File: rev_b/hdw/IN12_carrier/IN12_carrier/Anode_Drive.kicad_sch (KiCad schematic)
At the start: 36 parts, among them Q1001 MMSTA92, Q1002 MMSTA92, Q1003 MMSTA42, Q1004 MMSTA42, Q1005 MMSTA92, Q1006 MMSTA92, Q1007 MMSTA42, Q1008 MMSTA42, Q1009 MMSTA92, Q1010 MMSTA92, Q1011 MMSTA42, Q1012 MMSTA42

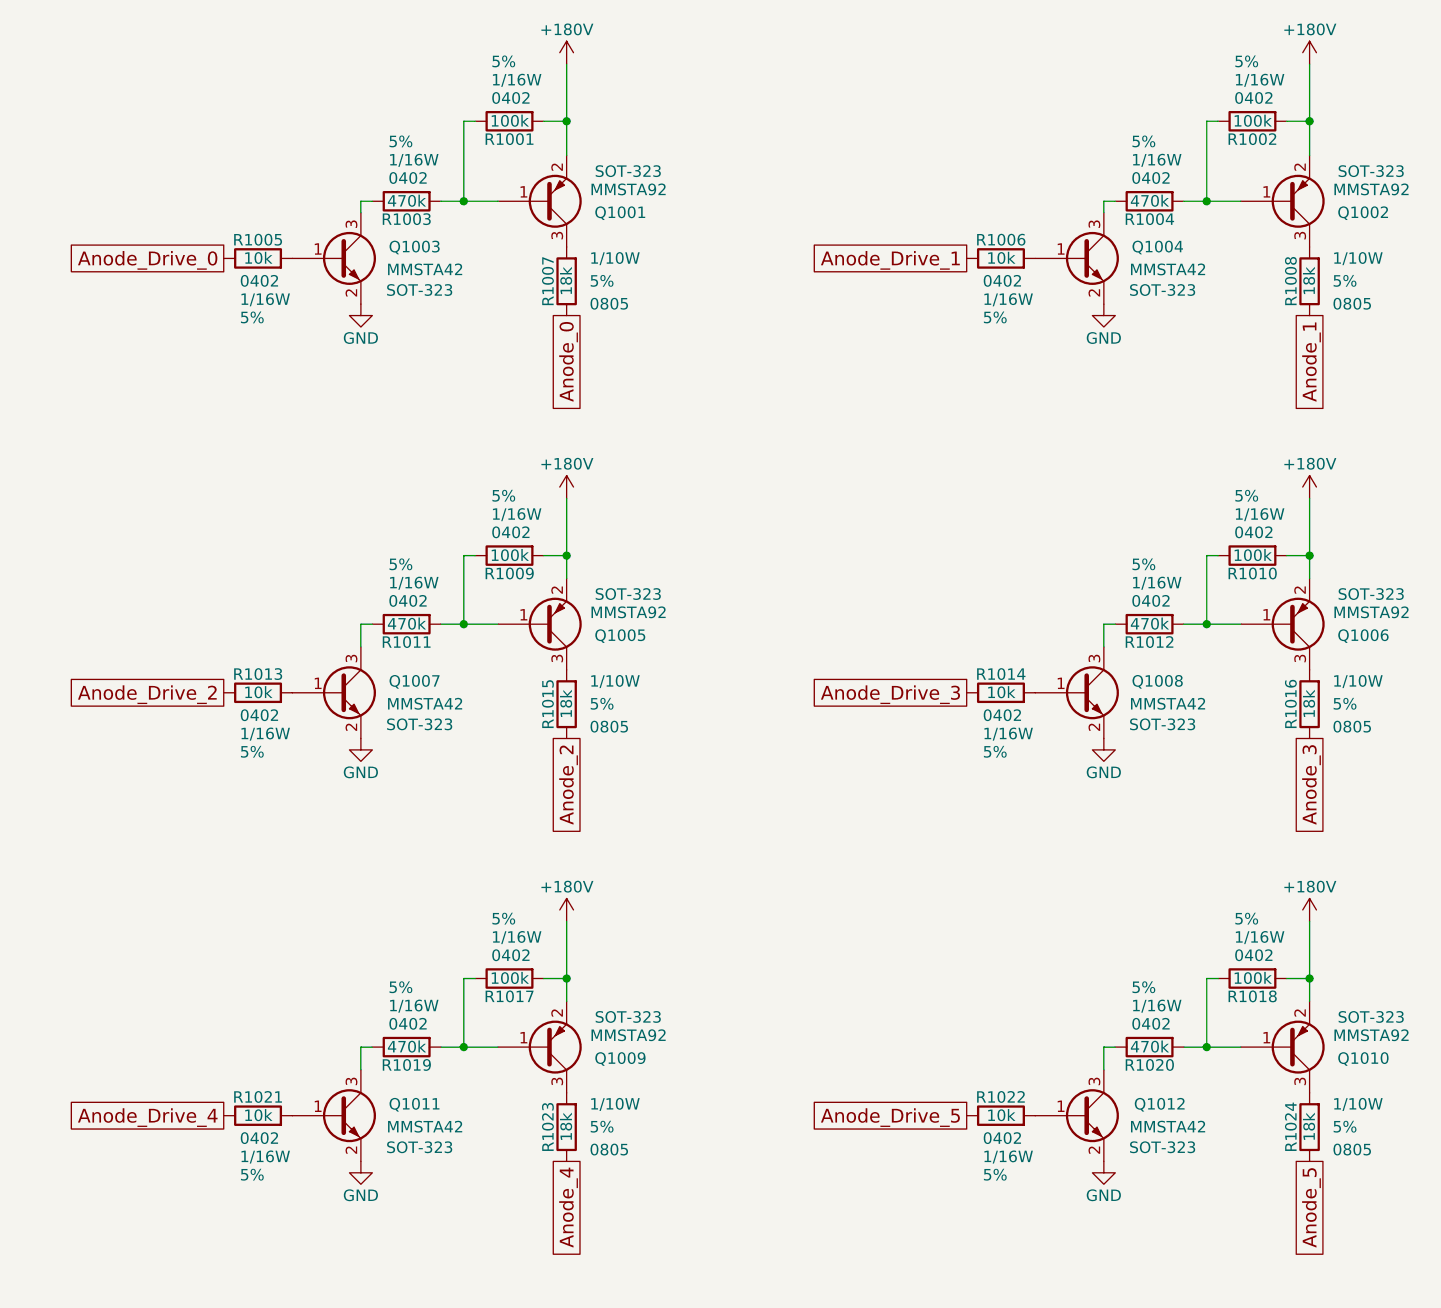
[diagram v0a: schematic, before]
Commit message: updated footprints, ran some DRC
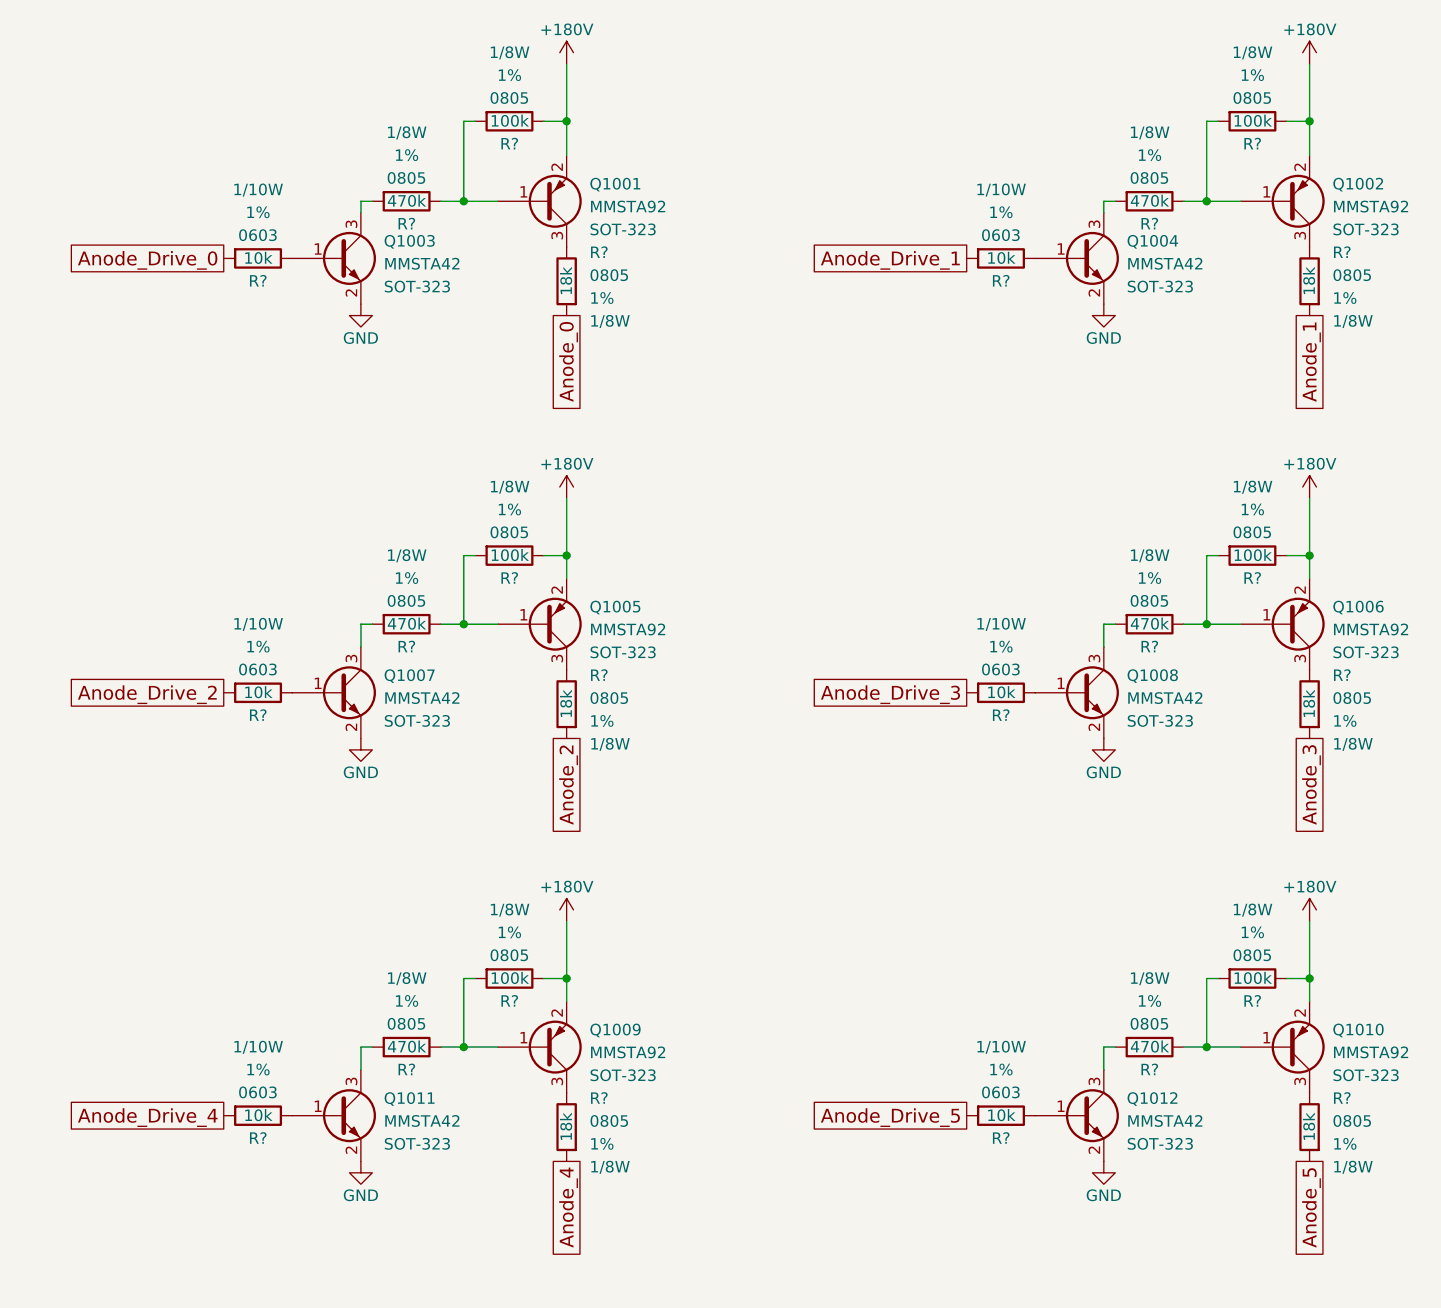
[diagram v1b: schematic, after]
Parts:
- removed R1001, R1002, R1009, R1010, R1017, R1018: 100k, Resistors_SMD:R_0402, symbol Nixie-Clock-rescue:R
- removed R1003, R1004, R1011, R1012, R1019, R1020: 470k, Resistors_SMD:R_0402, symbol Nixie-Clock-rescue:R
- removed R1005, R1006, R1013, R1014, R1021, R1022: 10k, Resistors_SMD:R_0402, symbol Nixie-Clock-rescue:R
- removed R1007, R1008, R1015, R1016, R1023, R1024: 18k, Resistors_SMD:R_0805, symbol Nixie-Clock-rescue:R
- added R? (x6): 470k, Resistors_SMD:R_0805, symbol Custom Library:R_Custom
- added R? (x6): 18k, Resistors_SMD:R_0805, symbol Custom Library:R_Custom
- added R? (x6): 10k, Resistors_SMD:R_0603, symbol Custom Library:R_Custom
- added R? (x6): 100k, Resistors_SMD:R_0805, symbol Custom Library:R_Custom
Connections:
- net +180V: now also R?.2, R?.2, R?.2, R?.2, R?.2, R?.2
- net Anode_0: now also R?.1
- net Anode_1: now also R?.1
- net Anode_2: now also R?.1
- net Anode_3: now also R?.1
- net Anode_4: now also R?.1
- net Anode_5: now also R?.1
- net Anode_Drive_0: now also R?.1
- net Anode_Drive_1: now also R?.1
- net Anode_Drive_2: now also R?.1
- net Anode_Drive_3: now also R?.1
- net Anode_Drive_4: now also R?.1
- net Anode_Drive_5: now also R?.1
- net at Q1010.1 (B): now also R?.1, R?.2
- net at Q1009.3 (C): now also R?.2
- net at Q1005.1 (B): now also R?.1, R?.2
- net at Q1008.1 (B): now also R?.2
- net at Q1008.3 (C): now also R?.1
- net at Q1005.3 (C): now also R?.2
- net at Q1009.1 (B): now also R?.1, R?.2
- net at Q1004.3 (C): now also R?.1
- net at Q1002.1 (B): now also R?.1, R?.2
- net at Q1002.3 (C): now also R?.2
- net at Q1003.1 (B): now also R?.2
- net at Q1003.3 (C): now also R?.1
- net at Q1007.3 (C): now also R?.1
- net at Q1011.3 (C): now also R?.1
- net at Q1011.1 (B): now also R?.2
- net at Q1007.1 (B): now also R?.2
- net at Q1006.3 (C): now also R?.2
- net at Q1006.1 (B): now also R?.1, R?.2
- net at Q1001.1 (B): now also R?.1, R?.2
- net at Q1004.1 (B): now also R?.2
- net at Q1012.3 (C): now also R?.1
- net at Q1010.3 (C): now also R?.2
- net at Q1001.3 (C): now also R?.2
- net at Q1012.1 (B): now also R?.2

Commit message: annotated, started arranging parts for IN12 carrier
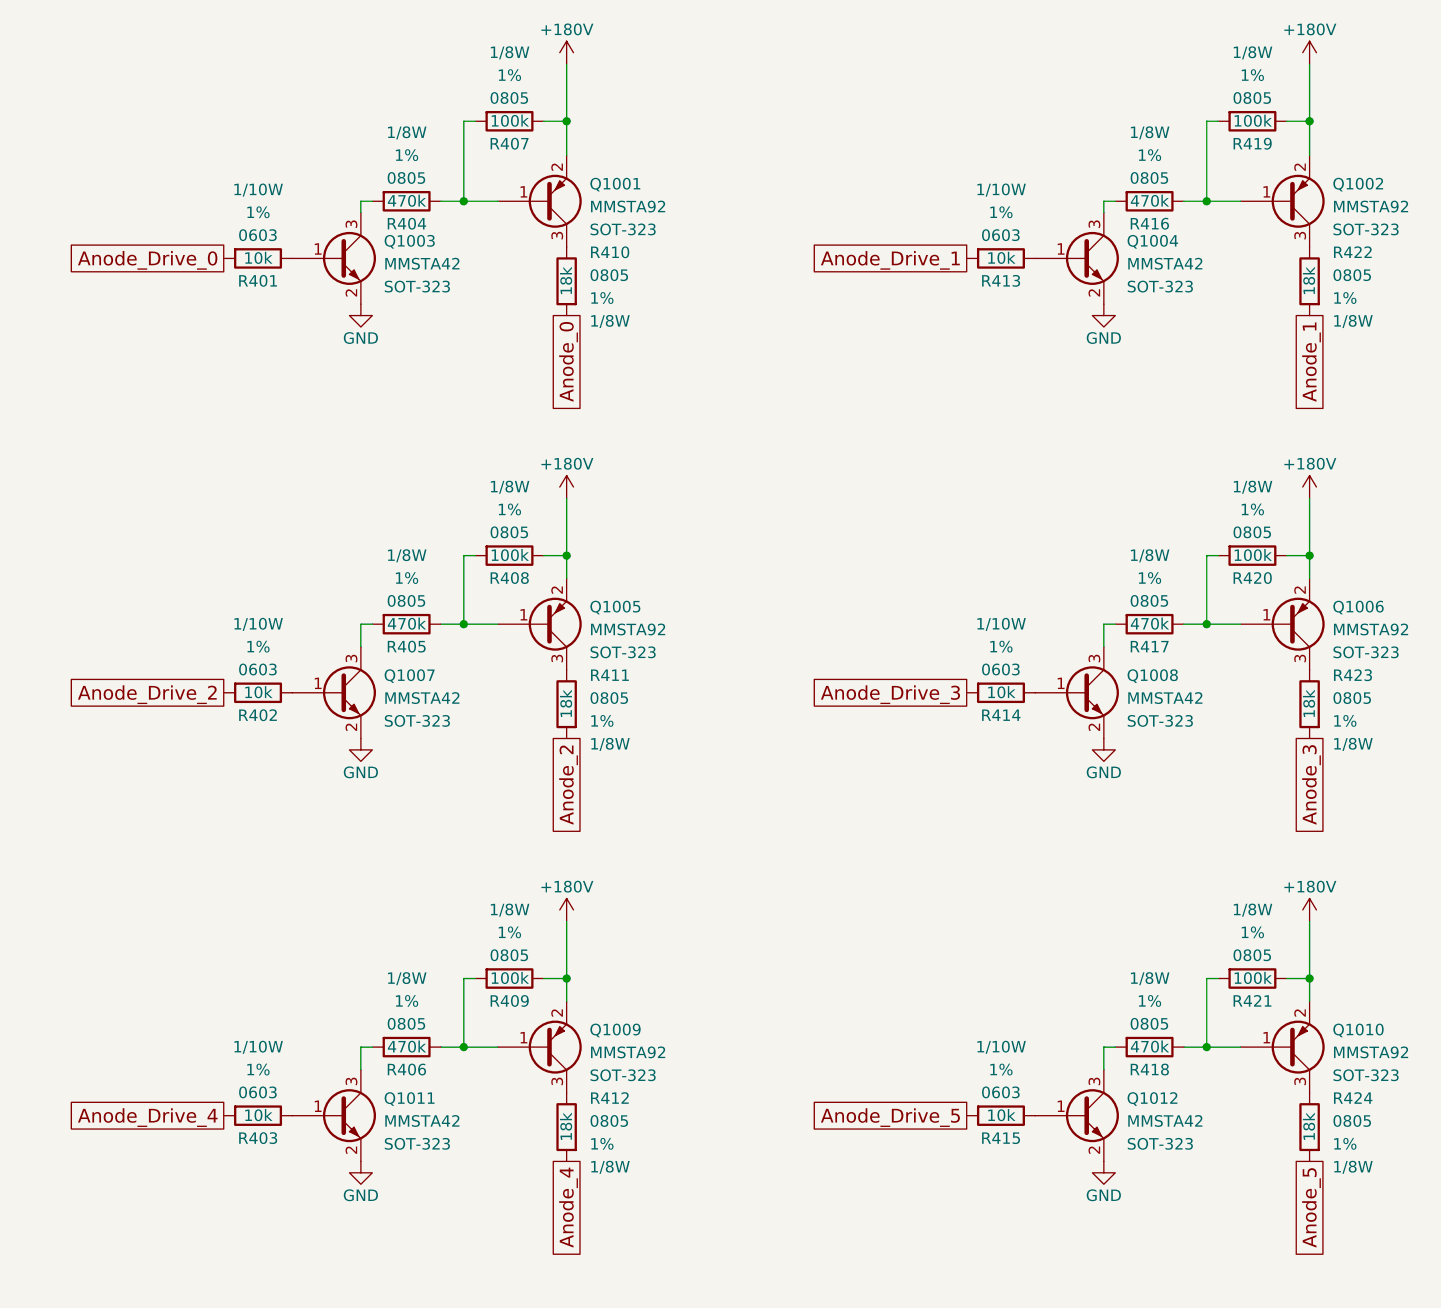
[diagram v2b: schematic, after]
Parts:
- gave numbers to parts that had none: 24

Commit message: lots of placement progress on IN12 carrier board
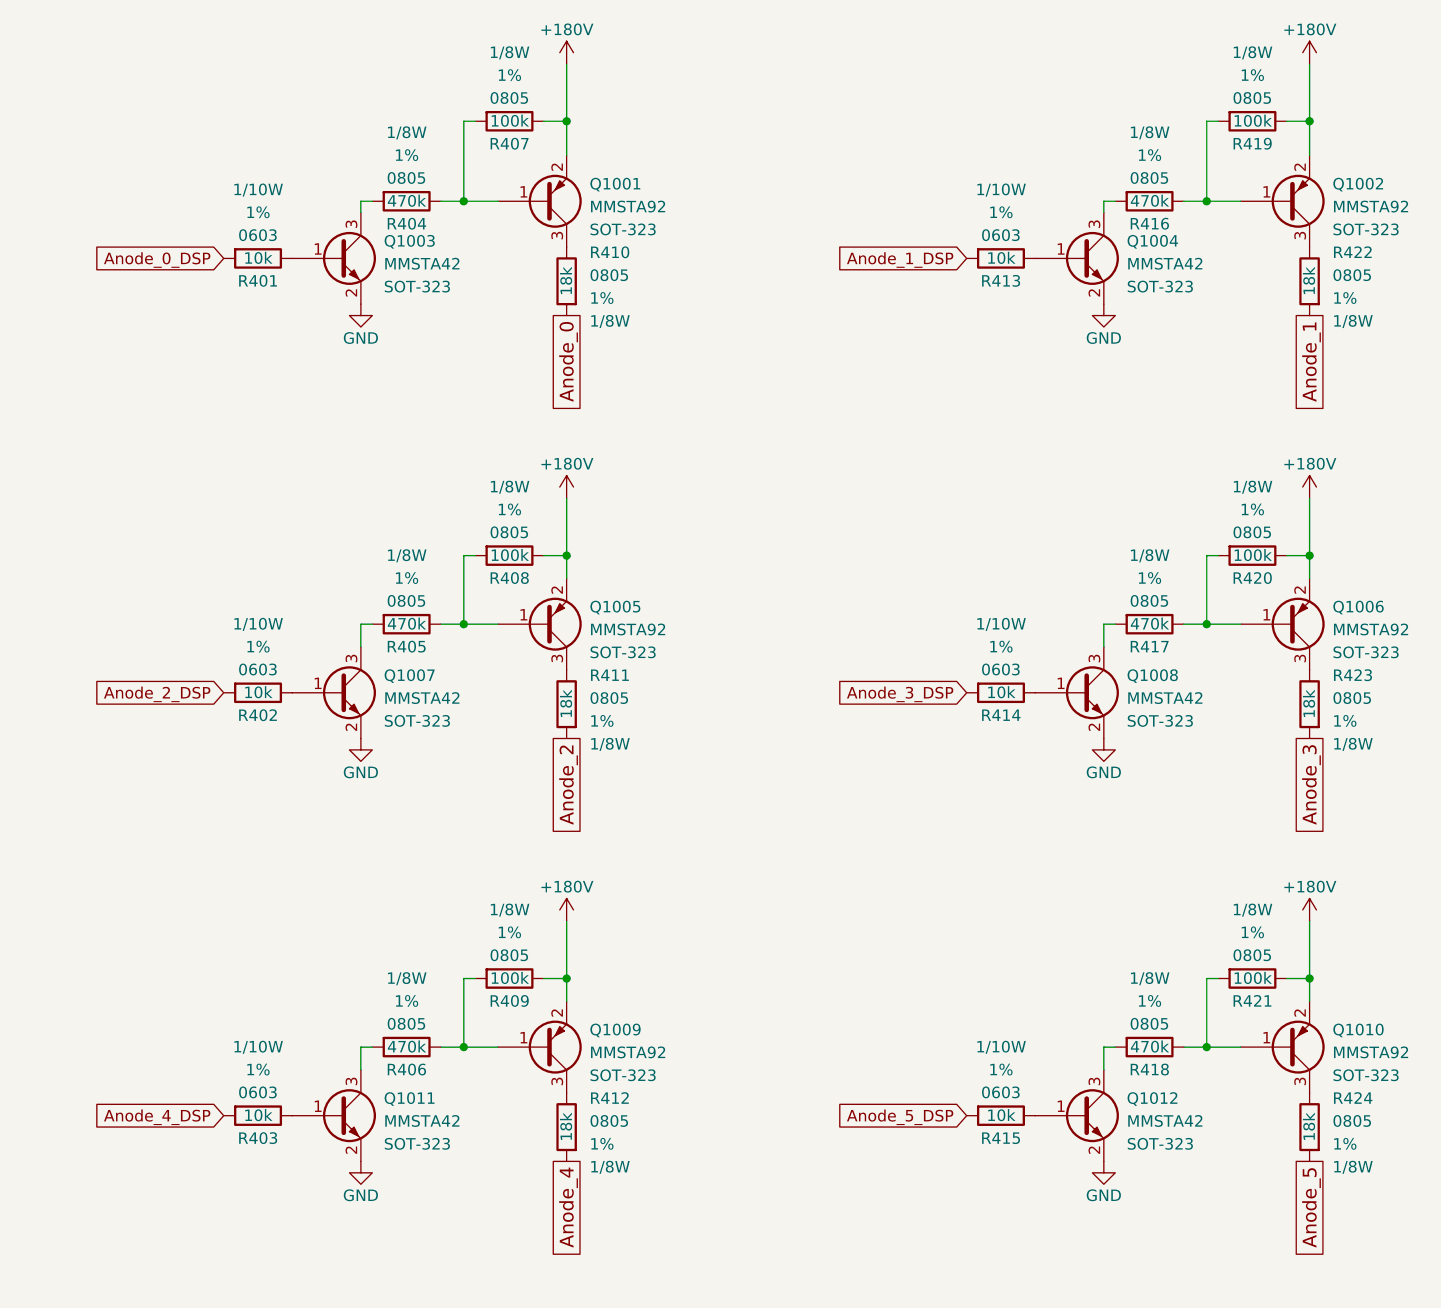
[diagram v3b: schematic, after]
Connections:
- net Anode_Drive_0 renamed Anode_0_DSP
- net Anode_Drive_1 renamed Anode_1_DSP
- net Anode_Drive_2 renamed Anode_2_DSP
- net Anode_Drive_3 renamed Anode_3_DSP
- net Anode_Drive_4 renamed Anode_4_DSP
- net Anode_Drive_5 renamed Anode_5_DSP
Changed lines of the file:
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@@
     )
   )
-  (global_label "Anode_Drive_2" (shape passive) (at 58.42 97.79 180)
-    (effects (font (size 1.524 1.524)) (justify right))
-    (property "Intersheetrefs" "${INTERSHEET_REFS}" (at 58.42 97.79 0)
-      (effects (font (size 1.27 1.27)) hide)
+  (global_label "Anode_5_DSP" (shape input) (at 140.97 144.78 180) (fields_autoplaced)
+    (effects (font (size 1.27 1.27)) (justify right))
+    (property "Intersheetrefs" "${INTERSHEET_REFS}" (at 125.5458 144.78 0)
+      (effects (font (size 1.27 1.27)) (justify right) hide)
     )
   )
-  (global_label "Anode_Drive_4" (shape passive) (at 58.42 144.78 180)
-    (effects (font (size 1.524 1.524)) (justify right))
-    (property "Intersheetrefs" "${INTERSHEET_REFS}" (at 58.42 144.78 0)
-      (effects (font (size 1.27 1.27)) hide)
+  (global_label "Anode_1_DSP" (shape input) (at 140.97 49.53 180) (fields_autoplaced)
+    (effects (font (size 1.27 1.27)) (justify right))
+    (property "Intersheetrefs" "${INTERSHEET_REFS}" (at 125.5458 49.53 0)
+      (effects (font (size 1.27 1.27)) (justify right) hide)
     )
   )
-  (global_label "Anode_Drive_3" (shape passive) (at 140.97 97.79 180)
-    (effects (font (size 1.524 1.524)) (justify right))
-    (property "Intersheetrefs" "${INTERSHEET_REFS}" (at 140.97 97.79 0)
-      (effects (font (size 1.27 1.27)) hide)
+  (global_label "Anode_2_DSP" (shape input) (at 58.42 97.79 180) (fields_autoplaced)
+    (effects (font (size 1.27 1.27)) (justify right))
+    (property "Intersheetrefs" "${INTERSHEET_REFS}" (at 42.9958 97.79 0)
+      (effects (font (size 1.27 1.27)) (justify right) hide)
     )
   )
-  (global_label "Anode_Drive_1" (shape passive) (at 140.97 49.53 180)
-    (effects (font (size 1.524 1.524)) (justify right))
-    (property "Intersheetrefs" "${INTERSHEET_REFS}" (at 140.97 49.53 0)
-      (effects (font (size 1.27 1.27)) hide)
+  (global_label "Anode_4_DSP" (shape input) (at 58.42 144.78 180) (fields_autoplaced)
+    (effects (font (size 1.27 1.27)) (justify right))
+    (property "Intersheetrefs" "${INTERSHEET_REFS}" (at 42.9958 144.78 0)
+      (effects (font (size 1.27 1.27)) (justify right) hide)
     )
   )
-  (global_label "Anode_Drive_0" (shape passive) (at 58.42 49.53 180)
-    (effects (font (size 1.524 1.524)) (justify right))
-    (property "Intersheetrefs" "${INTERSHEET_REFS}" (at 58.42 49.53 0)
-      (effects (font (size 1.27 1.27)) hide)
+  (global_label "Anode_3_DSP" (shape input) (at 140.97 97.79 180) (fields_autoplaced)
+    (effects (font (size 1.27 1.27)) (justify right))
+    (property "Intersheetrefs" "${INTERSHEET_REFS}" (at 125.5458 97.79 0)
+      (effects (font (size 1.27 1.27)) (justify right) hide)
     )
   )
@@
     )
   )
-  (global_label "Anode_Drive_5" (shape passive) (at 140.97 144.78 180)
-    (effects (font (size 1.524 1.524)) (justify right))
-    (property "Intersheetrefs" "${INTERSHEET_REFS}" (at 140.97 144.78 0)
-      (effects (font (size 1.27 1.27)) hide)
+  (global_label "Anode_0_DSP" (shape input) (at 58.42 49.53 180) (fields_autoplaced)
+    (effects (font (size 1.27 1.27)) (justify right))
+    (property "Intersheetrefs" "${INTERSHEET_REFS}" (at 42.9958 49.53 0)
+      (effects (font (size 1.27 1.27)) (justify right) hide)
     )
   )
